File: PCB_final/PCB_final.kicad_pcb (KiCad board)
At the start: 2 copper layers, 85.2 x 92.8 mm, 116 parts, among them J1 02x30_Shift_Register_Connector, J2 02x30_ADC_Connector, J5 PicoPinSocketB, J6 PicoPinSocketA, U1 74HC595, U10 LM321, U2 74HC595, U3 74HC595, U4 74HC595, U5 74HC595, U6 74HC595, U7 74HC595, U8 MAX11643EEG, U9 MAX11643EEG

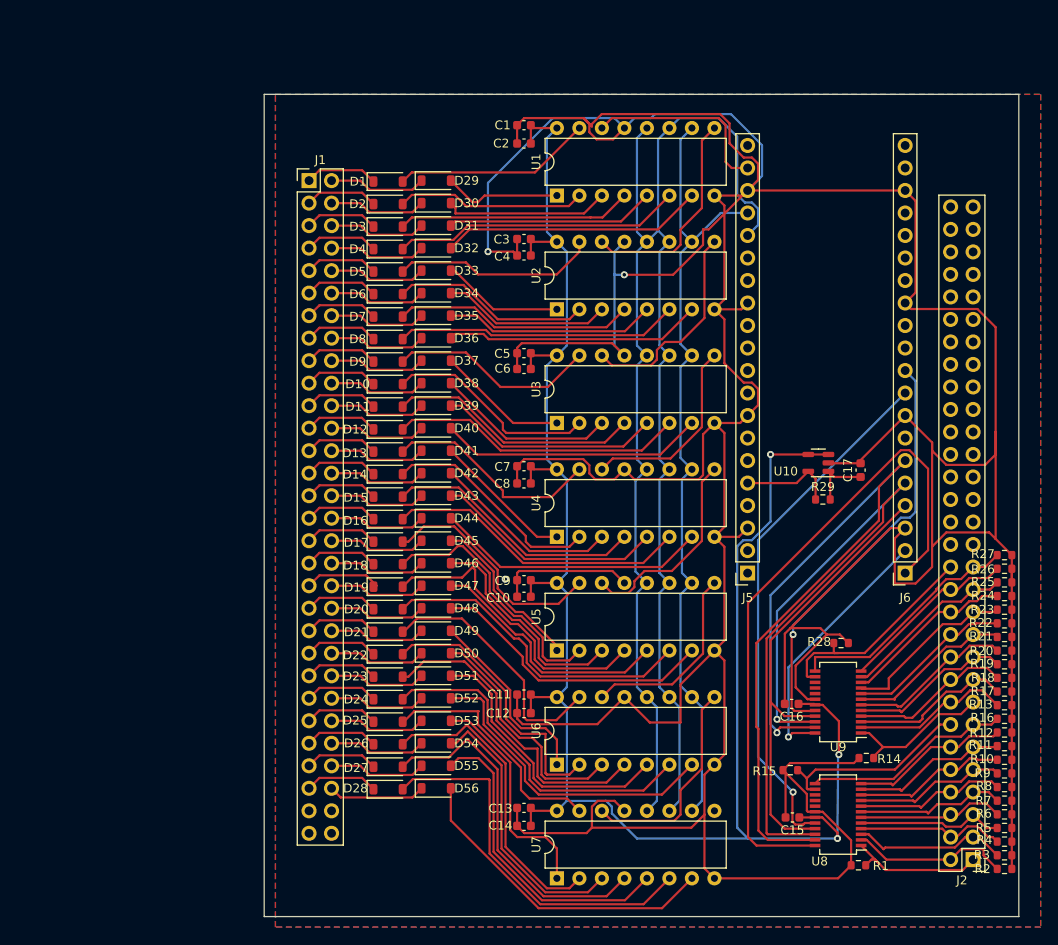
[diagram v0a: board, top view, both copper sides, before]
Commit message: fixed board edge
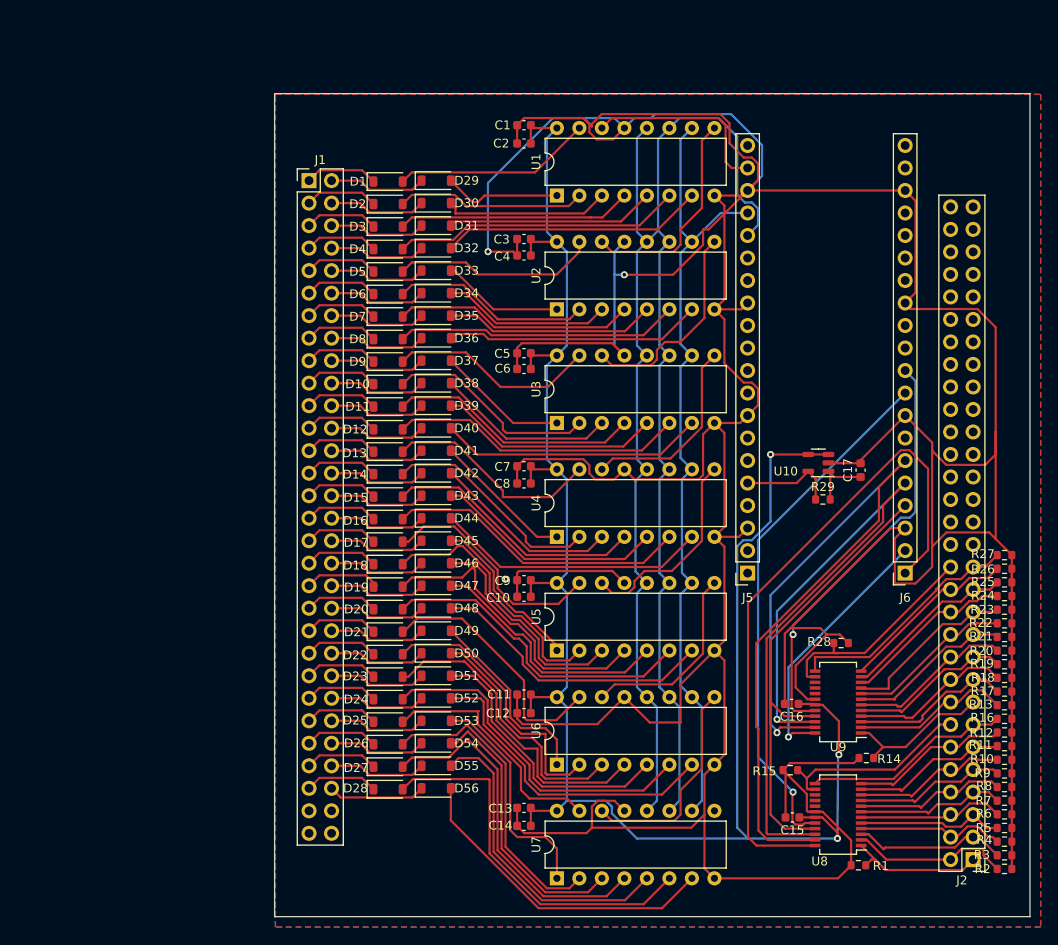
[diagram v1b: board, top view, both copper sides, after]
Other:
- board size 85.2 x 92.8 mm -> 85.2 x 92.9 mm
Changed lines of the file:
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@@
   )
   (setup
+    (stackup
+      (layer "F.SilkS" (type "Top Silk Screen"))
+      (layer "F.Paste" (type "Top Solder Paste"))
+      (layer "F.Mask" (type "Top Solder Mask") (thickness 0.01))
+      (layer "F.Cu" (type "copper") (thickness 0.035))
+      (layer "dielectric 1" (type "core") (thickness 1.51) (material "FR4") (epsilon_r 4.5) (loss_tangent 0.02))
+      (layer "B.Cu" (type "copper") (thickness 0.035))
+      (layer "B.Mask" (type "Bottom Solder Mask") (thickness 0.01))
+      (layer "B.Paste" (type "Bottom Solder Paste"))
+      (layer "B.SilkS" (type "Bottom Silk Screen"))
+      (copper_finish "None")
+      (dielectric_constraints no)
+    )
     (pad_to_mask_clearance 0)
     (pcbplotparams
@@
     )
   )
-  (gr_rect (start 120.655534 68.58) (end 205.817145 161.372196)
+  (gr_rect (start 121.827351 68.495196) (end 207.073393 161.379584)
     (stroke (width 0.1) (type default)) (fill none) (layer "Edge.Cuts"))
   (gr_text_box "RPI Pico\ngoes here\n\n:)))"

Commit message: Added PWR and GND planes to PCB
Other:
- copper layers 2 -> 4
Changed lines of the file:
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@@
   (layers
     (0 "F.Cu" signal)
+    (1 "In1.Cu" power "GND")
+    (2 "In2.Cu" power "PWR")
     (31 "B.Cu" signal)
     (32 "B.Adhes" user "B.Adhesive")
@@
       (layer "F.Mask" (type "Top Solder Mask") (thickness 0.01))
       (layer "F.Cu" (type "copper") (thickness 0.035))
-      (layer "dielectric 1" (type "core") (thickness 1.51) (material "FR4") (epsilon_r 4.5) (loss_tangent 0.02))
+      (layer "dielectric 1" (type "prepreg") (thickness 0.1) (material "FR4") (epsilon_r 4.5) (loss_tangent 0.02))
+      (layer "In1.Cu" (type "copper") (thickness 0.035))
+      (layer "dielectric 2" (type "core") (thickness 1.24) (material "FR4") (epsilon_r 4.5) (loss_tangent 0.02))
+      (layer "In2.Cu" (type "copper") (thickness 0.035))
+      (layer "dielectric 3" (type "prepreg") (thickness 0.1) (material "FR4") (epsilon_r 4.5) (loss_tangent 0.02))
       (layer "B.Cu" (type "copper") (thickness 0.035))
       (layer "B.Mask" (type "Bottom Solder Mask") (thickness 0.01))

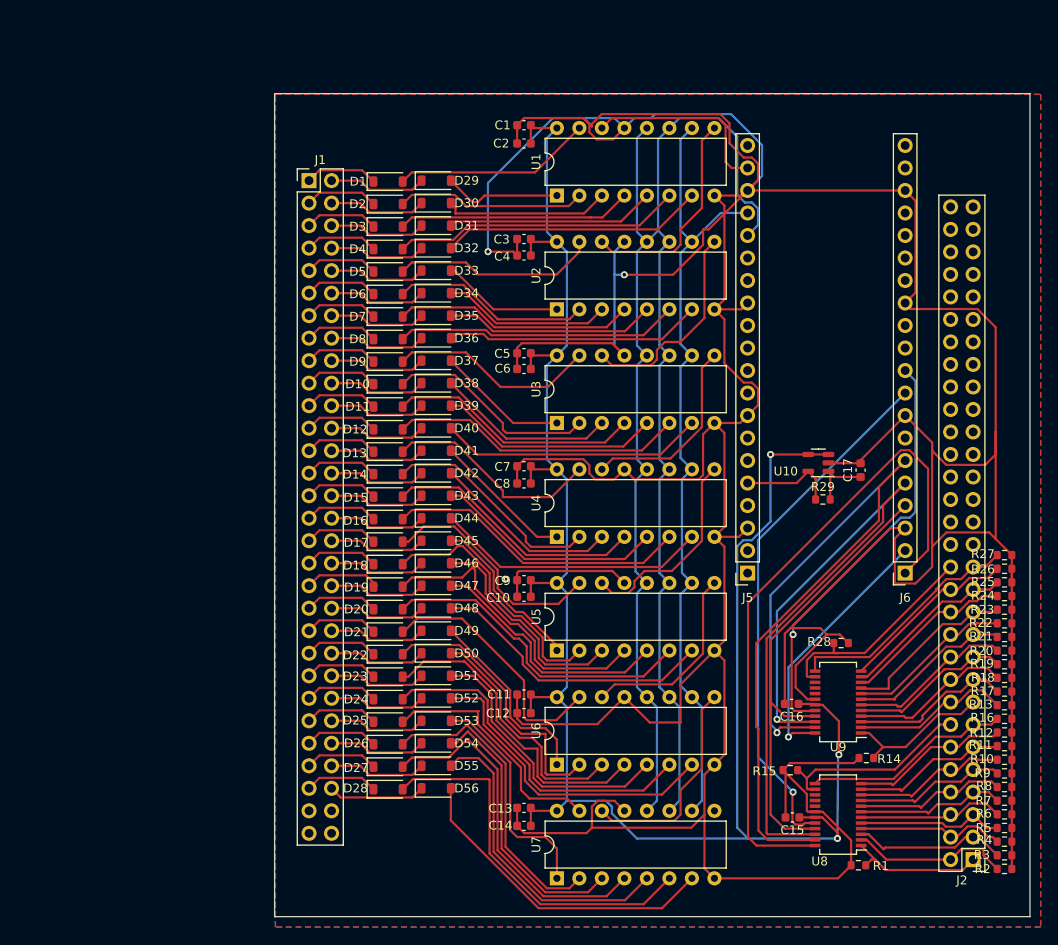
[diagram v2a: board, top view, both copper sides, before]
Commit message: PCB complete and redesigned w 4 layers. Passes desgin rule checker except for most of the silk screens. Schematic updated to connect adc unused pins to ground and beatified schematic
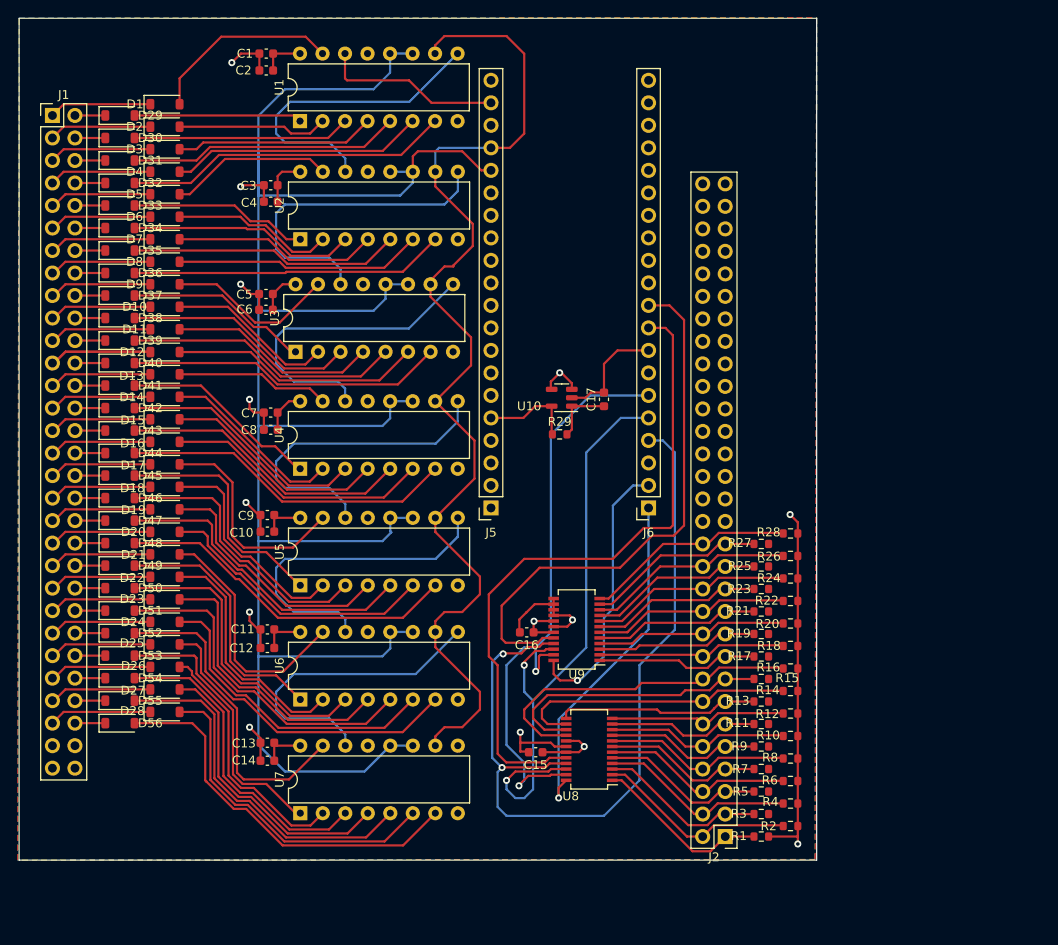
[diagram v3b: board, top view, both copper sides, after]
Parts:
- moved D55 36.4 mm to (104.4, 137.0)
- moved D29 36.4 mm to (104.4, 71.0)
- moved D30 36.4 mm to (104.4, 73.5)
- moved D31 36.4 mm to (104.4, 76.0)
- moved D32 36.4 mm to (104.4, 78.6)
- moved D33 36.4 mm to (104.4, 81.1)
- moved D34 36.4 mm to (104.4, 83.7)
- moved D35 36.4 mm to (104.4, 86.2)
- moved D36 36.4 mm to (104.4, 88.7)
- moved D37 36.4 mm to (104.4, 91.3)
- moved D38 36.4 mm to (104.4, 93.8)
- moved D39 36.4 mm to (104.4, 96.4)
- moved D40 36.4 mm to (104.4, 98.9)
- moved D41 36.4 mm to (104.4, 101.4)
- moved D42 36.4 mm to (104.4, 104.0)
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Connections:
- R13 pad 1: /Interface Board/ADC_IN16 -> /Interface Board/ADC_IN13
- R14 pad 1: /Interface Board/ADC_IN15 -> /Interface Board/ADC_IN14
- R15 pad 1: /Interface Board/ADC_IN14 -> /Interface Board/ADC_IN15
- R16 pad 1: /Interface Board/ADC_IN13 -> /Interface Board/ADC_IN16
- U8 pad 15: unconnected-(U8-AIN14-Pad15) -> /Interface Board/ADC_IN15
- U8 pad 16: unconnected-(U8-AIN15-Pad16) -> /Interface Board/ADC_IN16
- U8 pad 17: unconnected-(U8-REF-Pad17) -> +3V3
- U9 pad 1: /Interface Board/ADC_IN15 -> /Interface Board/ADC_IN17
- U9 pad 10: /Interface Board/ADC_IN24 -> /Interface Board/ADC_IN26
- U9 pad 11: /Interface Board/ADC_IN25 -> /Interface Board/ADC_IN27
- U9 pad 12: /Interface Board/ADC_IN26 -> /Interface Board/ADC_IN28
- U9 pad 13: /Interface Board/ADC_IN27 -> GND
- U9 pad 14: /Interface Board/ADC_IN28 -> GND
- U9 pad 15: unconnected-(U9-AIN14-Pad15) -> GND
- U9 pad 16: unconnected-(U9-AIN15-Pad16) -> GND
- U9 pad 17: unconnected-(U9-REF-Pad17) -> +3V3
- U9 pad 2: /Interface Board/ADC_IN16 -> /Interface Board/ADC_IN18
- U9 pad 3: /Interface Board/ADC_IN17 -> /Interface Board/ADC_IN19
- U9 pad 4: /Interface Board/ADC_IN18 -> /Interface Board/ADC_IN20
- U9 pad 5: /Interface Board/ADC_IN19 -> /Interface Board/ADC_IN21
- U9 pad 6: /Interface Board/ADC_IN20 -> /Interface Board/ADC_IN22
- U9 pad 7: /Interface Board/ADC_IN21 -> /Interface Board/ADC_IN23
- U9 pad 8: /Interface Board/ADC_IN22 -> /Interface Board/ADC_IN24
- U9 pad 9: /Interface Board/ADC_IN23 -> /Interface Board/ADC_IN25
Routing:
- net GND: track 618.4 -> 107.5 mm, vias 3 -> 11
- net +3V3: track 227.5 -> 53.1 mm
- net /Interface Board/SPI0_SCK: track 52.5 -> 92.7 mm, vias 0 -> 2
- net /Interface Board/SH_CLK: track 189.4 -> 229.0 mm
- net /Interface Board/ADC1_EOC: track 75.6 -> 39.3 mm, vias 0 -> 1
- net /Interface Board/SH_CLR: track 90.8 -> 121.4 mm
- net /Interface Board/SPI0_RX: track 97.6 -> 68.7 mm, vias 1 -> 2
- net /Interface Board/ADC_IN16: track 17.8 -> 37.7 mm
- net /Interface Board/SPI0_TX: track 88.6 -> 70.1 mm, vias 1 -> 2
- net /Interface Board/CS0: track 59.6 -> 75.3 mm, vias 1 -> 0
- net Net-(U5-QH'): track 21.9 -> 37.5 mm
- net Net-(D12-K): track 8.30 -> 23.2 mm
- net /Interface Board/ADC_IN15: track 17.1 -> 31.6 mm
- net /Interface Board/CS1: track 47.8 -> 62.2 mm, vias 1 -> 0
- net /Interface Board/SER5: track 23.2 -> 37.2 mm
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- added copper zone on In2.Cu, net +3V3
- added copper zone on In1.Cu, net GND
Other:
- board size 85.2 x 92.9 mm -> 90 x 95 mm

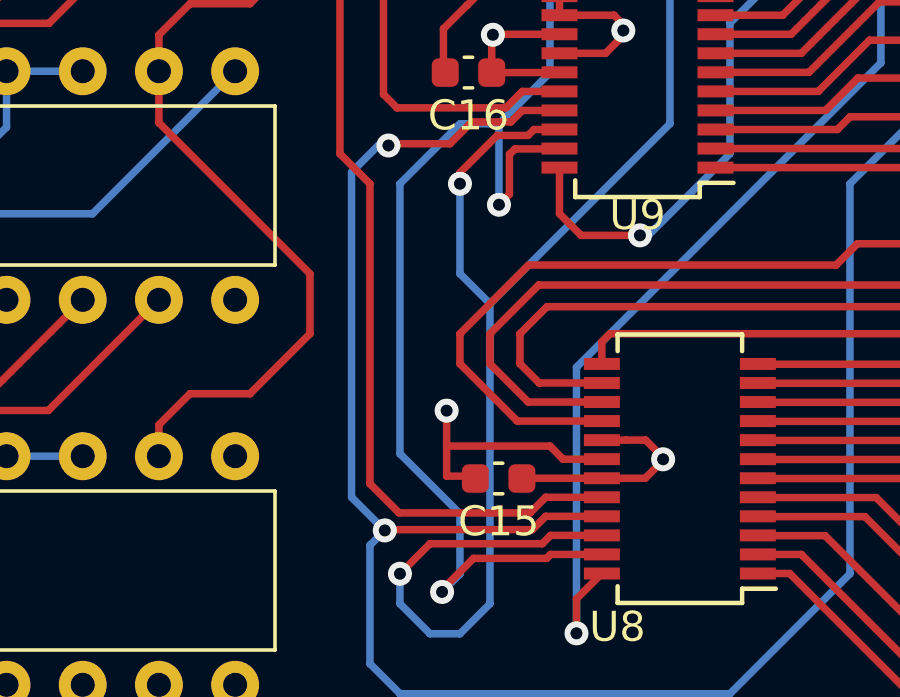
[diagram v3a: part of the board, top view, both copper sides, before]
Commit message: PCB silkscreen moved to stop warnings. Still getting a lot of seemingly unimportant errors from silkscreen. Updated design constraints to match manufacturer capabilities. Fixed a trace that was clipping a via.
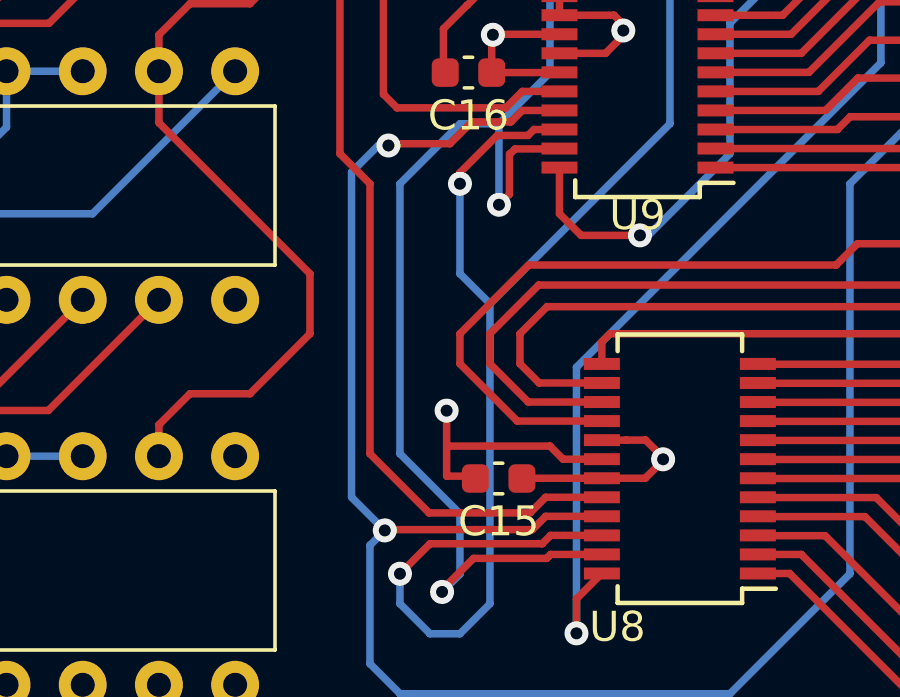
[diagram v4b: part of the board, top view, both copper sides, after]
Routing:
- net /Interface Board/CS0: track 75.3 -> 74.7 mm
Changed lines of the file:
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@@
     (stroke (width 0.15) (type solid))  )
   (gr_text_box "Pressure Matrix Interface Board"
-    (start 122.876473 69.616952) (end 138.116473 74.696952) (layer "F.SilkS")
+    (start 94.76 61.92) (end 110 67) (layer "F.SilkS")
       (effects (font (size 1 1) (thickness 0.15)) (justify left top))
     (stroke (width 0.15) (type solid))  )
@@
   (segment (start 153 107) (end 157.444859 102.555141) (width 0.25) (layer "B.Cu") (net 200))
   (segment (start 151.30033 133.69967) (end 151.30033 131) (width 0.25) (layer "B.Cu") (net 200))
+  (segment (start 166.48473 117.51527) (end 163.48473 117.51527) (width 0.25) (layer "F.Cu") (net 202))
+  (segment (start 166.777919 117.222081) (end 166.48473 117.51527) (width 0.25) (layer "F.Cu") (net 202))
+  (segment (start 164.030708 94.935141) (end 165.935141 94.935141) (width 0.25) (layer "F.Cu") (net 202))
   (segment (start 146 125) (end 146 132) (width 0.25) (layer "F.Cu") (net 202))
-  (segment (start 164.030708 94.935141) (end 165.935141 94.935141) (width 0.25) (layer "F.Cu") (net 202))
+  (segment (start 147 142) (end 148.971316 143.971316) (width 0.25) (layer "F.Cu") (net 202))
+  (segment (start 152.336132 143.971316) (end 152.856508 143.45094) (width 0.25) (layer "F.Cu") (net 202))
   (segment (start 146 132) (end 147 133) (width 0.25) (layer "F.Cu") (net 202))
-  (segment (start 152.856508 143.45094) (end 154.73094 143.45094) (width 0.25) (layer "F.Cu") (net 202))
   (segment (start 165.935141 94.935141) (end 166.777919 95.777919) (width 0.25) (layer "F.Cu") (net 202))
-  (segment (start 163.48473 117.51527) (end 160 121) (width 0.25) (layer "F.Cu") (net 202))
-  (segment (start 166.48473 117.51527) (end 163.48473 117.51527) (width 0.25) (layer "F.Cu") (net 202))
-  (segment (start 160 121) (end 150 121) (width 0.25) (layer "F.Cu") (net 202))
-  (segment (start 147 143) (end 147.971316 143.971316) (width 0.25) (layer "F.Cu") (net 202))
-  (segment (start 166.777919 117.222081) (end 166.48473 117.51527) (width 0.25) (layer "F.Cu") (net 202))
   (segment (start 150 121) (end 146 125) (width 0.25) (layer "F.Cu") (net 202))
   (segment (start 166.777919 95.777919) (end 166.777919 117.222081) (width 0.25) (layer "F.Cu") (net 202))
-  (segment (start 147.971316 143.971316) (end 152.336132 143.971316) (width 0.25) (layer "F.Cu") (net 202))
-  (segment (start 147 133) (end 147 143) (width 0.25) (layer "F.Cu") (net 202))
-  (segment (start 152.336132 143.971316) (end 152.856508 143.45094) (width 0.25) (layer "F.Cu") (net 202))
+  (segment (start 147 133) (end 147 142) (width 0.25) (layer "F.Cu") (net 202))
+  (segment (start 163.48473 117.51527) (end 160 121) (width 0.25) (layer "F.Cu") (net 202))
+  (segment (start 160 121) (end 150 121) (width 0.25) (layer "F.Cu") (net 202))
+  (segment (start 152.856508 143.45094) (end 154.73094 143.45094) (width 0.25) (layer "F.Cu") (net 202))
+  (segment (start 148.971316 143.971316) (end 152.336132 143.971316) (width 0.25) (layer "F.Cu") (net 202))
   (segment (start 168.03884 117.224155) (end 168.03884 94.03884) (width 0.25) (layer "F.Cu") (net 203))
   (segment (start 152.078103 129.921897) (end 151.530649 130.46935) (width 0.25) (layer "F.Cu") (net 203))
